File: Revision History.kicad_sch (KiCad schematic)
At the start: 0 parts

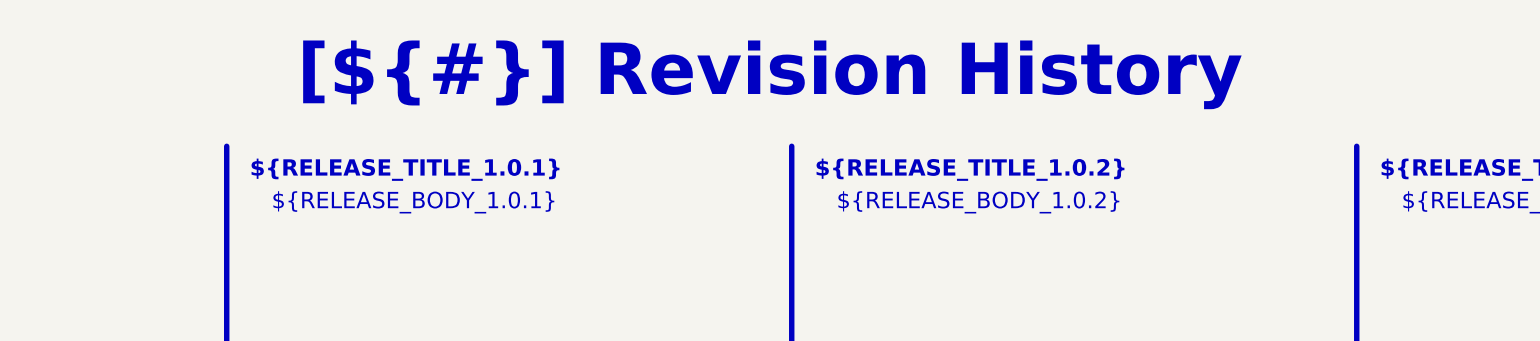
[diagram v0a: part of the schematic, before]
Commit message: feat: Added some design notes, fixed some values in line with sim
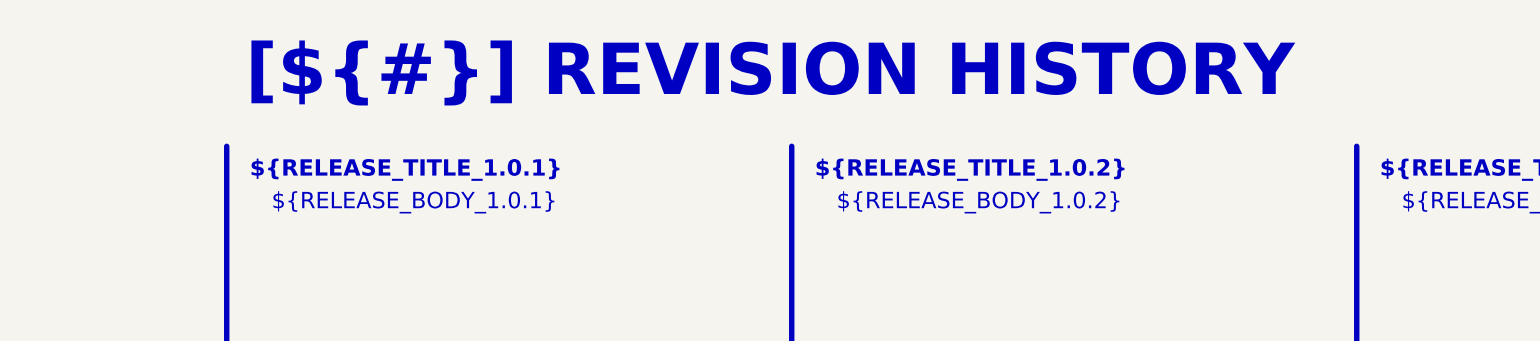
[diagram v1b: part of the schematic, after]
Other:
- title: Revision History -> REVISION HISTORY
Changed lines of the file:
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@@
 	(paper "A4")
 	(title_block
-		(title "Revision History")
+		(title "REVISION HISTORY")
 		(date "2025-01-12")
 		(rev "${REVISION}")
